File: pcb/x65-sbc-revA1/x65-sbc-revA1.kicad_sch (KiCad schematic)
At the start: 8 parts

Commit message: pcb sbc: more pcb work
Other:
- note added: "24AA025E48T"
- note added: "AURA FPGA"
- note added: "Amp."
- note added: "Audio Line output"
- note added: "CPU W65C816"
- note added: "DAC"
- note added: "D[0-7],CTRL"
- note added: "EUI EEPROM"
- note added: "Initial design based on MOBO+VABO rev001. PCB 180x100mm, 4-L."
- note added: "RJ45 for 10/100 Ethernet"
- note added: "SD-Card slot"
- note added: "Sound from VERA"
- note added: "Speaker mono"
- note added: "VERA FPGA"
- note added: "VGA output"
- note added: "W6100L LAN"
- note added: "X65 IS OPEN SOURCE => + VERILOG FPGA DESIGN + CIRCUIT SCHEMATIC + PCB LAYOUT + ORIGINAL SOFTWARE"
- note added: "revA1 / xx.1.2024"
- note removed: "(VIA to be folded in FPGA -> all PA/PB sigs are also connected to the NORA FPGA)"
- note removed: "- Video output by VERA FPGA (Frank van den Hoef) iCE40UP5K - SD-Card slot by VERA - audio - ??? - Ethernet port RJ45 by Wiznet"
- note removed: "2x 2x10-pin headers"
- note removed: "A[0-3]"
- note removed: "CPU W65C02 / 816"
- note removed: "CTRL"
- note removed: "Initial design. PCB 100x100mm, 2-L. First PCB production: PCBWAY on 29.3.2023 file: openx65-mobo-rev01b-grb.zip"
- note removed: "Original VIA"
- note removed: "Video/Audio board (separate scm)"
- note removed: "W65C22"
- note removed: "rev01 / 30.3.2023"
- moved on the sheet: FID101, FID102, FID103, FID104, H101, H102, H103, H104

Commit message: x65-sbc: pcb done
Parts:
- added SYM101: Logo_Open_Hardware_Large, Symbol:OSHW-Logo2_7.3x6mm_SilkScreen, symbol Graphic:Logo_Open_Hardware_Large
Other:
- note added: "X65 IS OPEN SOURCE: + CIRCUIT SCHEMATIC + PCB LAYOUT + VERILOG FPGA DESIGN + TOOLS USED + ORIGINAL SOFTWARE"
- note added: "revA1 / 12.1.2024"
- note removed: "X65 IS OPEN SOURCE => + VERILOG FPGA DESIGN + CIRCUIT SCHEMATIC + PCB LAYOUT + ORIGINAL SOFTWARE"
- note removed: "revA1 / xx.1.2024"
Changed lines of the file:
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@@
   (title_block
     (title "X65-SBC")
-    (date "2023-12-29")
+    (date "2024-01-10")
     (rev "revA1")
     (company "FOR X65.EU DESIGNED BY JSYKORA.INFO")
@@
     (stroke (width 0) (type default))
   )
-  (polyline (pts (xy 120.015 104.775) (xy 118.11 104.775))
+  (polyline (pts (xy 120.015 105.41) (xy 118.11 105.41))
     (stroke (width 0) (type solid))
   )
@@
     (stroke (width 0) (type default))
   )
-  (polyline (pts (xy 118.11 104.775) (xy 118.11 97.155))
+  (polyline (pts (xy 118.11 105.41) (xy 118.11 97.155))
     (stroke (width 0) (type solid))
   )
@@
     (stroke (width 0) (type default))
     (fill (type none))
+  )
+  (text_box "Important Links:\nx65.eu\nwww.jsykora.info\ngithub.com/jsyk/x65"
+    (at 81.915 172.72 0) (size 40.005 20.32)
+    (stroke (width 0) (type default))
+    (fill (type none))
+    (effects (font (size 2 2)) (justify left top))
   )
   (text "Amp." (at 110.49 142.24 0)
@@
     (effects (font (size 1.27 1.27)) (justify left bottom))
   )
-  (text "revA1 / xx.1.2024" (at 125.73 66.04 0)
+  (text "revA1 / 12.1.2024" (at 125.73 66.04 0)
     (effects (font (size 1.27 1.27)) (justify left bottom))
   )
@@
     (effects (font (size 5 5)) (justify left bottom))
   )
-  (text "X65 IS\nOPEN SOURCE =>\n+ VERILOG FPGA DESIGN\n+ CIRCUIT SCHEMATIC\n+ PCB LAYOUT\n+ ORIGINAL SOFTWARE"
+  (text "X65 IS\nOPEN SOURCE:\n+ CIRCUIT SCHEMATIC\n+ PCB LAYOUT\n+ VERILOG FPGA DESIGN\n+ TOOLS USED\n+ ORIGINAL SOFTWARE"
     (at 137.16 194.31 0)
     (effects (font (size 2 2) (thickness 0.254) bold (color 132 0 0 1)) (justify left bottom))
@@
   (symbol (lib_id "power:GND") (at 40.64 187.96 0) (unit 1)
     (in_bom yes) (on_board yes) (dnp no) (fields_autoplaced)
-    (property "Reference" "#PWR0207" (at 40.64 194.31 0)
+    (property "Reference" "#PWR01" (at 40.64 194.31 0)
       (effects (font (size 1.27 1.27)) hide)
     )
@@
     (instances
       (project "x65-sbc-revA1"
-        (path "/85750bea-43a1-4629-9575-611e72af7f9f/9c40083a-a45d-4b41-ab0a-cc2b752c6926"
-          (reference "#PWR0207") (unit 1)
-        )
         (path "/85750bea-43a1-4629-9575-611e72af7f9f"
           (reference "#PWR01") (unit 1)
@@
     )
   )
-  (symbol (lib_id "Graphic:Logo_Open_Hardware_Large") (at 160.02 168.275 0) (unit 1)
+  (symbol (lib_id "Graphic:Logo_Open_Hardware_Large") (at 159.385 165.1 0) (unit 1)
     (in_bom no) (on_board yes) (dnp no) (fields_autoplaced)
-    (property "Reference" "#SYM101" (at 160.02 155.575 0)
-      (effects (font (size 1.27 1.27)) hide)
-    )
-    (property "Value" "Logo_Open_Hardware_Large" (at 160.02 178.435 0)
-      (effects (font (size 1.27 1.27)) hide)
-    )
-    (property "Footprint" "Symbol:OSHW-Logo2_7.3x6mm_SilkScreen" (at 160.02 168.275 0)
-      (effects (font (size 1.27 1.27)) hide)
-    )
-    (property "Datasheet" "~" (at 160.02 168.275 0)
-      (effects (font (size 1.27 1.27)) hide)
-    )
-    (property "Sim.Enable" "0" (at 160.02 168.275 0)
-      (effects (font (size 1.27 1.27)) hide)
-    )
-    (instances
-      (project "x65-sbc-revA1"
-        (path "/85750bea-43a1-4629-9575-611e72af7f9f"
-          (reference "#SYM101") (unit 1)
-        )
-      )
+    (property "Reference" "SYM101" (at 159.385 152.4 0)
+      (effects (font (size 1.27 1.27)) hide)
+    )
+    (property "Value" "Logo_Open_Hardware_Large" (at 159.385 175.26 0)
+      (effects (font (size 1.27 1.27)) hide)
+    )
+    (property "Footprint" "Symbol:OSHW-Logo2_7.3x6mm_SilkScreen" (at 159.385 165.1 0)
+      (effects (font (size 1.27 1.27)) hide)
+    )
+    (property "Datasheet" "~" (at 159.385 165.1 0)
+      (effects (font (size 1.27 1.27)) hide)
+    )
+    (property "Sim.Enable" "0" (at 159.385 165.1 0)
+      (effects (font (size 1.27 1.27)) hide)
+    )
+    (instances
+      (project "x65-sbc-revA1"
+        (path "/85750bea-43a1-4629-9575-611e72af7f9f"
+          (reference "SYM101") (unit 1)
+        )
+      )

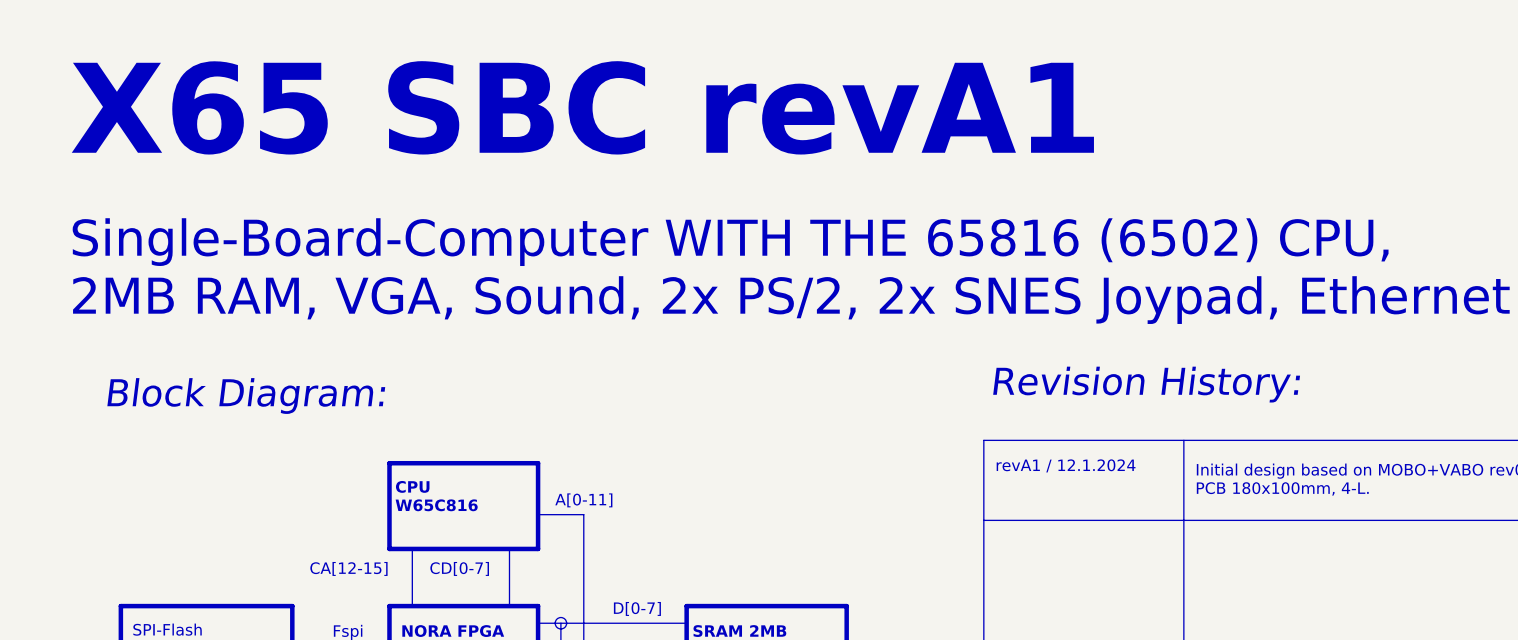
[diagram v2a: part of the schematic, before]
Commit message: pcb/scm x65-sbc update
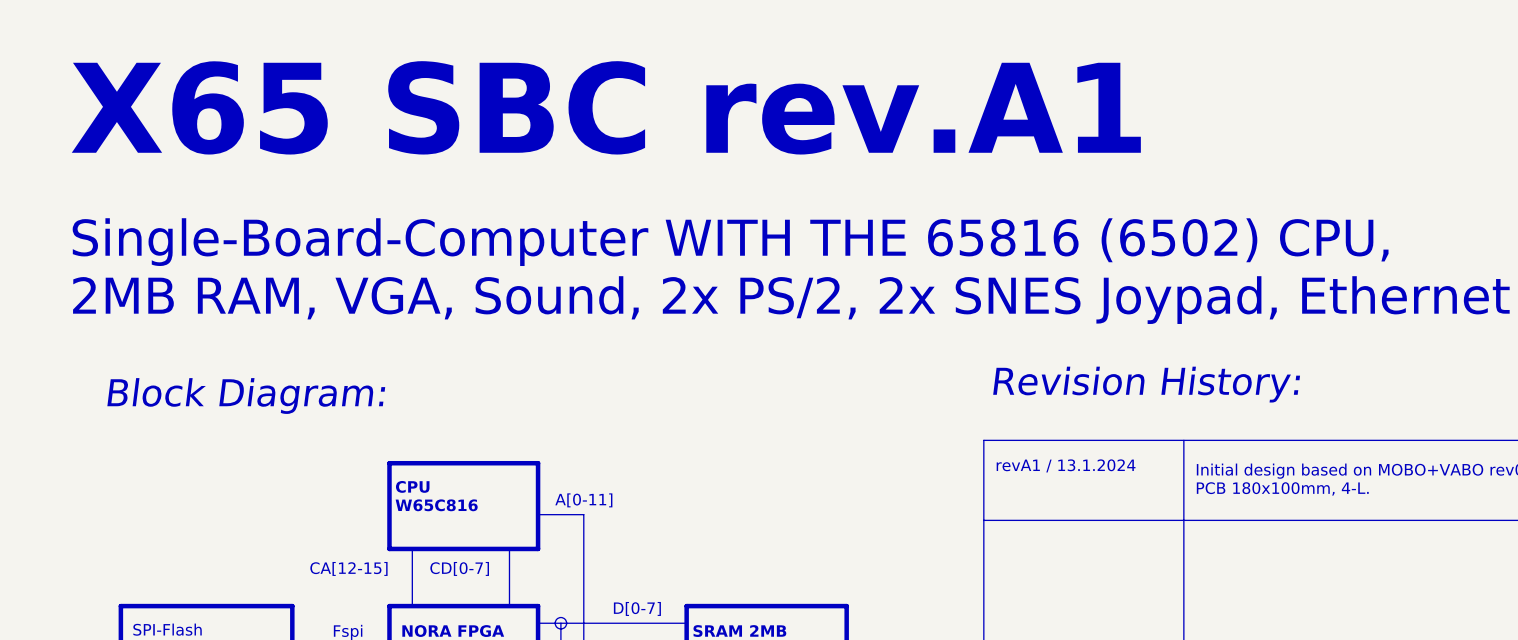
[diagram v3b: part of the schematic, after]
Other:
- note added: "X65 SBC rev.A1"
- note added: "revA1 / 13.1.2024"
- note removed: "X65 SBC revA1"
- note removed: "revA1 / 12.1.2024"
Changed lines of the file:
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@@
     (effects (font (size 5 5)) (justify left bottom))
   )
-  (text "X65 SBC revA1" (at 22.86 31.75 0)
+  (text "X65 SBC rev.A1" (at 22.86 31.75 0)
     (effects (font (size 10 10) (thickness 2) bold) (justify left bottom))
   )
@@
     (effects (font (size 1.27 1.27)) (justify left bottom))
   )
-  (text "revA1 / 12.1.2024" (at 125.73 66.04 0)
+  (text "revA1 / 13.1.2024" (at 125.73 66.04 0)
     (effects (font (size 1.27 1.27)) (justify left bottom))
   )
